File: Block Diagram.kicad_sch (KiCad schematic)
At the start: 0 parts

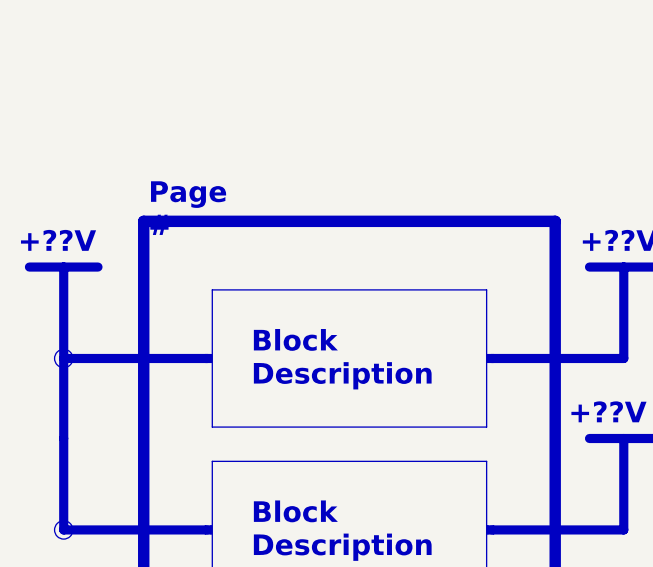
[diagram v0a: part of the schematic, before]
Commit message: Add device schematic symbols and packages
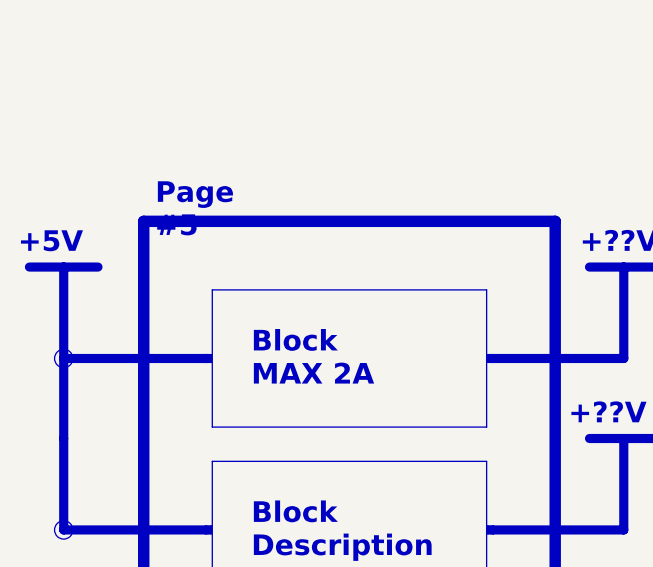
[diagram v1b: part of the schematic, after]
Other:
- note added: "+5V"
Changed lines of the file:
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@@
 		)
 	)
-	(text_box "Page #"
-		(exclude_from_sim no)
-		(at 65.278 68.58 0)
-		(size 13.97 5.08)
-		(stroke
-			(width -0.0001)
-			(type default)
-		)
-		(fill
-			(type none)
-		)
-		(effects
-			(font
-				(face "Times New Roman")
-				(size 2.286 2.286)
-				(thickness 0.4572)
-				(bold yes)
-				(color 0 0 0 1)
-			)
-			(justify left top)
+	(text_box "Page #5"
+		(exclude_from_sim no)
+		(at 66.04 68.58 0)
+		(size 15.24 5.08)
+		(stroke
+			(width -0.0001)
+			(type default)
+		)
+		(fill
+			(type none)
+		)
+		(effects
+			(font
+				(face "Times New Roman")
+				(size 2.286 2.286)
+				(thickness 0.4572)
+				(bold yes)
+				(color 0 0 0 1)
+			)
+			(justify left top)
+			(href "#5")
 		)
 	)
@@
 		)
 	)
-	(text_box "Block\nDescription"
+	(text_box "Block\nMAX 2A"
 		(exclude_from_sim no)
 		(at 76.708 85.09 0)
@@
 		)
 	)
-	(text "+??V"
+	(text "+5V"
 		(exclude_from_sim no)
 		(at 52.578 78.74 0)
